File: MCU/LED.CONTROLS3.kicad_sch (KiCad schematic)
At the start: 22 parts, among them U10 LM5012DDAR, U8 HHG1D-1, U9 AMC1301DWVR

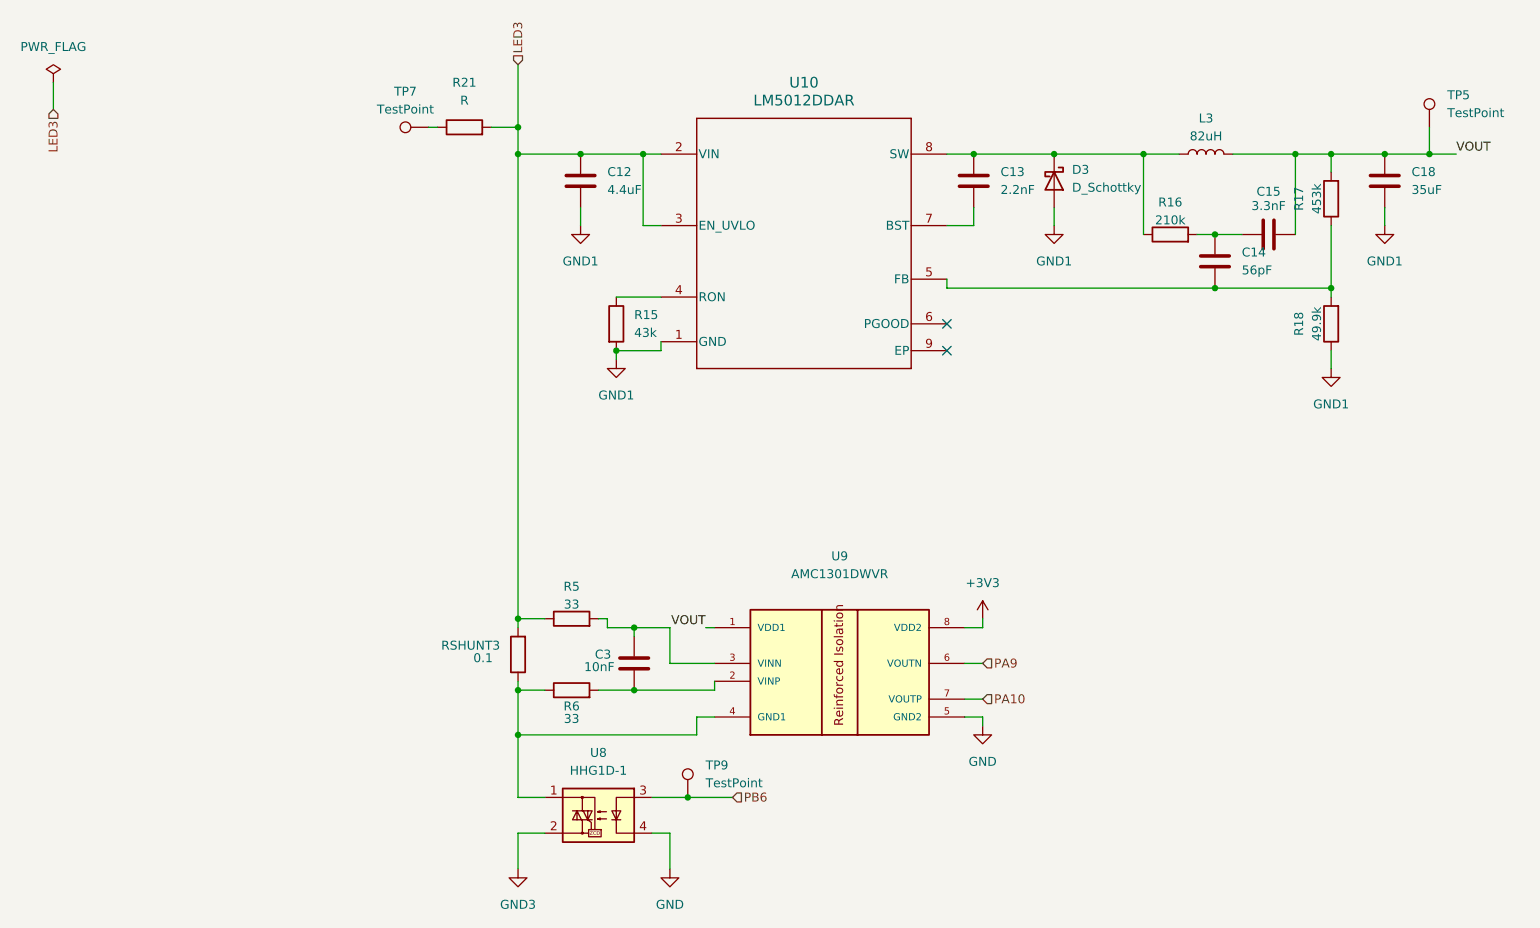
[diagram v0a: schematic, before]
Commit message: Centralized isolation amp power source. Corrected STM32 pins.
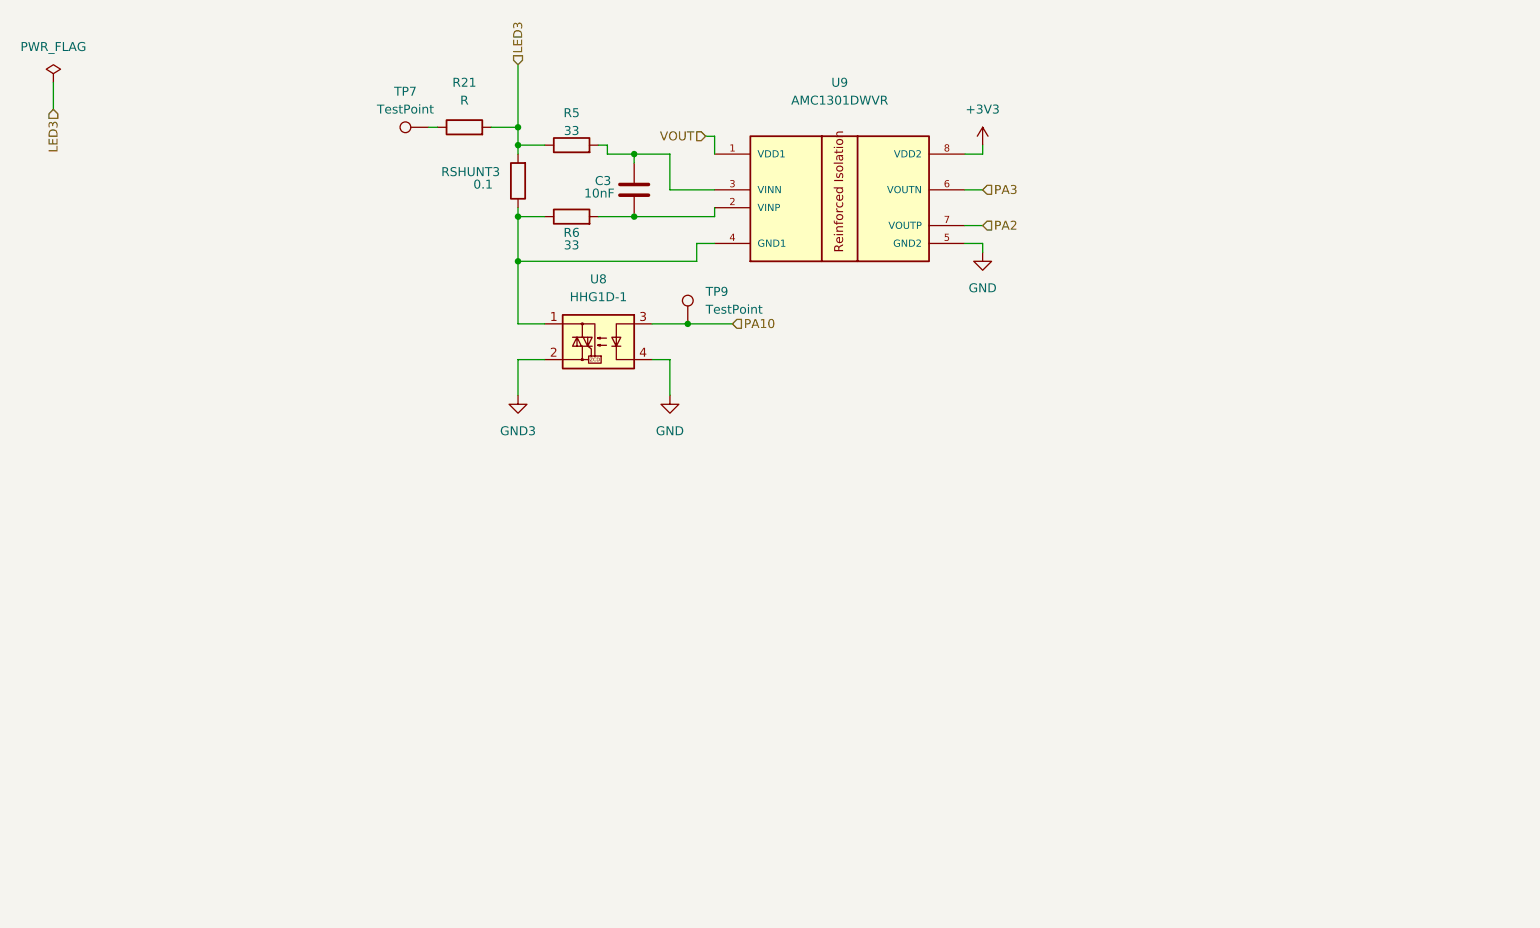
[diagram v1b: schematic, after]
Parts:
- removed C12: 4.4uF, symbol Device:C
- removed C13: 2.2nF, symbol Device:C
- removed C14: 56pF, symbol Device:C
- removed C15: 3.3nF, symbol Device:C
- removed C18: 35uF, symbol Device:C
- removed D3: D_Schottky, symbol Device:D_Schottky
- removed L3: 82uH, symbol Device:L
- removed R15: 43k, symbol Device:R
- removed R16: 210k, Resistor_SMD:R_1812_4532Metric_Pad1.30x3.40mm_HandSolder, symbol Device:R
- removed R17: 453k, Resistor_SMD:R_1812_4532Metric_Pad1.30x3.40mm_HandSolder, symbol Device:R
- removed R18: 49.9k, Resistor_SMD:R_1812_4532Metric_Pad1.30x3.40mm_HandSolder, symbol Device:R
- removed TP5: TestPoint, symbol Connector:TestPoint
- removed U10: LM5012DDAR, DDA0008E-IPC_A, symbol LM 5012 Buck Converter:LM5012DDAR
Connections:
- net PB6 is gone; now on net PA10: TP9.1, U8.3
- net PA10: no longer U9.7 (VOUTP)
- net PA9 renamed PA3
- new net PA2: U9.7 (VOUTP)
- no-connect marks 2 -> 0
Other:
- moved on the sheet: C3, R5, R6, RSHUNT3, TP9, U8, U9

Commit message: Assigned footprints and added RTD
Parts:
- removed R21: R, symbol Device:R
- C3: footprint (none) -> Capacitor_SMD:C_1206_3216Metric
- TP7: value TestPoint -> Post_LED3_Test; footprint (none) -> TestPoint:TestPoint_Pad_2.0x2.0mm
- TP9: value TestPoint -> LED3_MCU_CT; footprint (none) -> TestPoint:TestPoint_Pad_1.5x1.5mm
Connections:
- net LED3: now also TP7.1
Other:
- moved on the sheet: TP7

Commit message: Finalized schematic and started layout
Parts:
- U9: footprint AMC1301DWVR:SOIC127P1150X280-8N -> AMC1301 Isolated Amplifier:DWV0008A
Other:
- moved on the sheet: C3, R5, R6, RSHUNT3, TP7, TP9, U8, U9
